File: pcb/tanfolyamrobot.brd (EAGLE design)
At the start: 81.3 x 58.7 mm, 84 parts, among them IC1 STM32F10XRXT6, IC2 7805, IC4 FT232RL, IC5 LD117AS33TR, M1 DRV8833, Q1 AO4407A, Q2 BSS123, Q3 BSS123, Q4 BSS123, X1 CSTCE08M, X2 PWR

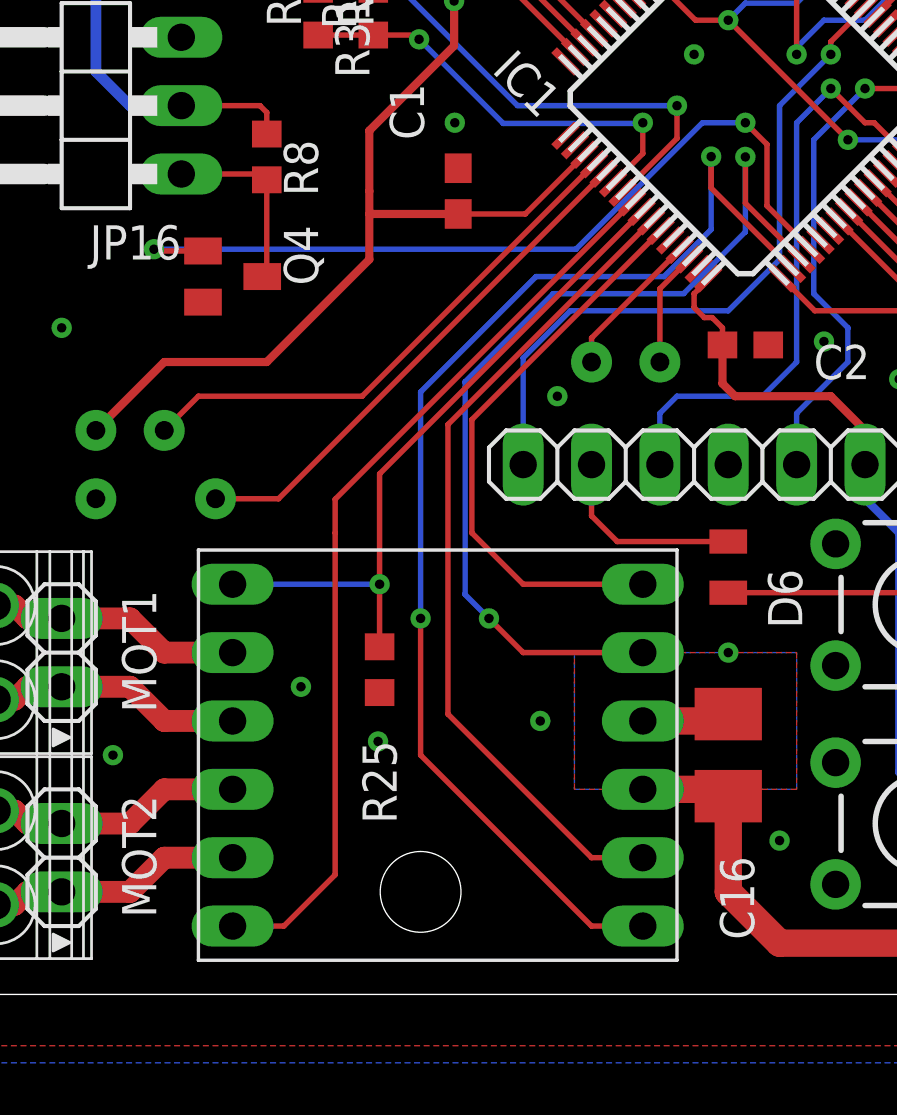
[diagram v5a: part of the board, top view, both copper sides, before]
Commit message: added battery voltage measurement (#1)
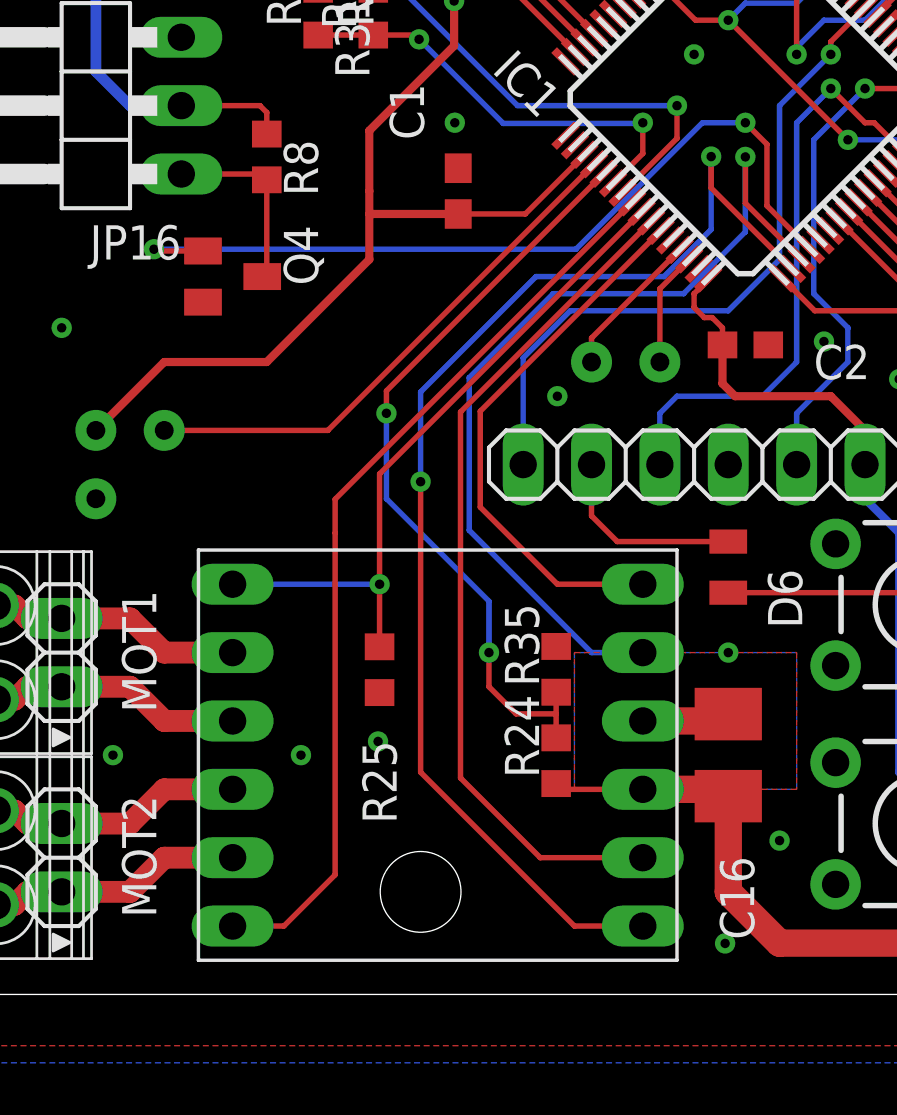
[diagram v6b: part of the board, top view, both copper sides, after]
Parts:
- added R24: 27K, rcl:R0603
- added R35: 6K8, rcl:R0603
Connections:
- removed net PA5: IC1.21
- new net VCC_SENSE: IC1.21, R24.2, R35.1
- net GND: now also R35.2
- net VCC: now also R24.1
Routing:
- net VCC_SENSE: track 0.00 -> 28.6 mm, vias 0 -> 2
- net PA5: track 19.4 -> 0.00 mm, vias 1 -> 0
- net VCC: track 96.3 -> 99.6 mm
- net MOTOR2_IN1: track 35.6 -> 34.0 mm, vias 2 -> 1
- net MOTOR2_IN2: track 21.3 -> 20.3 mm
- net MOTOR1_IN2: track 30.9 -> 31.6 mm
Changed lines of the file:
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@@
 <attribute name="VALUE" x="18.415" y="49.19345" size="1.27" layer="27" rot="R90"/>
+</element>
+<element name="R24" library="rcl" library_urn="urn:adsk.eagle:library:334" package="R0603" package3d_urn="urn:adsk.eagle:package:23555/3" value="27K" x="25.35555" y="8.683625" smashed="yes" rot="R90">
+<attribute name="NAME" x="24.72055" y="8.048625" size="1.27" layer="25" rot="R90"/>
+<attribute name="POPULARITY" value="70" x="25.35555" y="8.683625" size="1.778" layer="27" rot="R90" display="off"/>
+<attribute name="SPICEPREFIX" value="R" x="25.35555" y="8.683625" size="1.778" layer="27" rot="R90" display="off"/>
+<attribute name="VALUE" x="27.26055" y="8.048625" size="1.27" layer="27" rot="R90"/>
+</element>
+<element name="R35" library="rcl" library_urn="urn:adsk.eagle:library:334" package="R0603" package3d_urn="urn:adsk.eagle:package:23555/3" value="6K8" x="25.35555" y="12.0777" smashed="yes" rot="R90">
+<attribute name="NAME" x="24.72055" y="11.4427" size="1.27" layer="25" rot="R90"/>
+<attribute name="POPULARITY" value="70" x="25.35555" y="12.0777" size="1.778" layer="27" rot="R90" display="off"/>
+<attribute name="SPICEPREFIX" value="R" x="25.35555" y="12.0777" size="1.778" layer="27" rot="R90" display="off"/>
+<attribute name="VALUE" x="27.26055" y="11.4427" size="1.27" layer="27" rot="R90"/>
 </element>
 </elements>
@@
 <via x="8.255" y="18.415" extent="1-16" drill="0.7" diameter="1.524"/>
 <via x="6.985" y="38.1" extent="1-16" drill="0.35"/>
-<via x="15.875" y="11.43" extent="1-16" drill="0.35"/>
+<via x="15.875" y="8.89" extent="1-16" drill="0.35"/>
 <via x="18.73885" y="9.398" extent="1-16" drill="0.35"/>
-<via x="24.765" y="10.16" extent="1-16" drill="0.35"/>
+<via x="31.632525" y="1.895475" extent="1-16" drill="0.35"/>
 <via x="31.75" y="12.7" extent="1-16" drill="0.35"/>
 <via x="33.655" y="5.715" extent="1-16" drill="0.35"/>
@@
 <contactref element="R33" pad="2"/>
 <via x="21.59" y="32.385" extent="1-16" drill="0.35"/>
+<contactref element="R35" pad="2"/>
 </signal>
 <signal name="+3V3">
@@
 <wire x1="69.85" y1="23.2918" x2="69.85" y2="21.59" width="0.4064" layer="1"/>
 <wire x1="71.12" y1="23.2918" x2="71.12" y2="20.955" width="0.4064" layer="1"/>
+<contactref element="R24" pad="1"/>
+<wire x1="25.35555" y1="7.833625" x2="25.569175" y2="7.62" width="0.2032" layer="1"/>
+<wire x1="25.569175" y1="7.62" x2="28.575" y2="7.62" width="0.2032" layer="1"/>
 </signal>
 <signal name="N$14">
@@
 <contactref element="M1" pad="IN1"/>
 <via x="31.115" y="31.1277" extent="1-16" drill="0.35"/>
-<via x="20.32" y="13.97" extent="1-16" drill="0.35"/>
-<wire x1="28.575" y1="2.54" x2="26.67" y2="2.54" width="0.2032" layer="1"/>
-<wire x1="20.32" y1="8.89" x2="20.32" y2="13.97" width="0.2032" layer="1"/>
-<wire x1="26.67" y1="2.54" x2="20.32" y2="8.89" width="0.2032" layer="1"/>
+<via x="20.32" y="19.05" extent="1-16" drill="0.35"/>
+<wire x1="28.575" y1="2.54" x2="26.035" y2="2.54" width="0.2032" layer="1"/>
+<wire x1="20.32" y1="8.255" x2="20.32" y2="19.05" width="0.2032" layer="1"/>
+<wire x1="26.035" y1="2.54" x2="20.32" y2="8.255" width="0.2032" layer="1"/>
 <contactref element="IC1" pad="34"/>
 <wire x1="31.115" y1="31.1277" x2="31.115" y2="29.956828125" width="0.2032" layer="1"/>
@@
 <wire x1="24.609425" y1="26.67" x2="29.365575" y2="26.67" width="0.2032" layer="16"/>
 <wire x1="31.115" y1="28.419425" x2="31.115" y2="31.1277" width="0.2032" layer="16"/>
-<wire x1="20.32" y1="13.97" x2="20.32" y2="22.380575" width="0.2032" layer="16"/>
+<wire x1="20.32" y1="19.05" x2="20.32" y2="22.380575" width="0.2032" layer="16"/>
 <wire x1="29.365575" y1="26.67" x2="31.115" y2="28.419425" width="0.2032" layer="16"/>
 </signal>
@@
 <contactref element="M1" pad="IN2"/>
 <contactref element="IC1" pad="26"/>
-<wire x1="21.336" y1="10.414" x2="26.67" y2="5.08" width="0.2032" layer="1"/>
-<wire x1="26.67" y1="5.08" x2="28.575" y2="5.08" width="0.2032" layer="1"/>
-<wire x1="28.88481875" y1="28.722184375" x2="21.336" y2="21.173365625" width="0.2032" layer="1"/>
-<wire x1="21.336" y1="21.173365625" x2="21.336" y2="10.414" width="0.2032" layer="1"/>
+<wire x1="21.802725" y1="8.042275" x2="24.765" y2="5.08" width="0.2032" layer="1"/>
+<wire x1="24.765" y1="5.08" x2="28.575" y2="5.08" width="0.2032" layer="1"/>
+<wire x1="28.88481875" y1="28.722184375" x2="21.802725" y2="21.640090625" width="0.2032" layer="1"/>
+<wire x1="21.802725" y1="21.640090625" x2="21.802725" y2="8.042275" width="0.2032" layer="1"/>
 </signal>
 <signal name="MOTOR2_IN1">
 <contactref element="M1" pad="IN3"/>
-<wire x1="28.575" y1="12.7" x2="24.13" y2="12.7" width="0.2032" layer="1"/>
-<wire x1="24.13" y1="12.7" x2="22.86" y2="13.97" width="0.2032" layer="1"/>
-<via x="22.86" y="13.97" extent="1-16" drill="0.35"/>
 <via x="32.385" y="31.115" extent="1-16" drill="0.35"/>
-<wire x1="22.86" y1="13.97" x2="21.971" y2="14.859" width="0.2032" layer="16"/>
 <contactref element="IC1" pad="35"/>
 <wire x1="32.385" y1="31.115" x2="32.385" y2="29.393934375" width="0.2032" layer="1"/>
 <wire x1="34.4709625" y1="27.307971875" x2="32.385" y2="29.393934375" width="0.2032" layer="1"/>
-<wire x1="21.971" y1="22.761575" x2="25.244425" y2="26.035" width="0.2032" layer="16"/>
+<wire x1="22.126575" y1="22.91715" x2="25.244425" y2="26.035" width="0.2032" layer="16"/>
 <wire x1="25.244425" y1="26.035" x2="30.09265" y2="26.035" width="0.2032" layer="16"/>
 <wire x1="32.385" y1="28.32735" x2="30.09265" y2="26.035" width="0.2032" layer="16"/>
 <wire x1="32.385" y1="28.32735" x2="32.385" y2="31.115" width="0.2032" layer="16"/>
-<wire x1="21.971" y1="14.859" x2="21.971" y2="22.761575" width="0.2032" layer="16"/>
+<wire x1="22.126575" y1="17.243425" x2="22.126575" y2="22.91715" width="0.2032" layer="16"/>
+<wire x1="28.575" y1="12.7" x2="26.67" y2="12.7" width="0.2032" layer="16"/>
+<wire x1="26.67" y1="12.7" x2="22.126575" y2="17.243425" width="0.2032" layer="16"/>
 </signal>
 <signal name="MOTOR2_IN2">
 <contactref element="M1" pad="IN4"/>
 <contactref element="IC1" pad="27"/>
-<wire x1="28.575" y1="15.24" x2="24.13" y2="15.24" width="0.2032" layer="1"/>
-<wire x1="29.238371875" y1="28.36863125" x2="22.225" y2="21.355259375" width="0.2032" layer="1"/>
-<wire x1="22.225" y1="21.355259375" x2="22.225" y2="17.145" width="0.2032" layer="1"/>
-<wire x1="22.225" y1="17.145" x2="24.13" y2="15.24" width="0.2032" layer="1"/>
+<wire x1="28.575" y1="15.24" x2="25.4" y2="15.24" width="0.2032" layer="1"/>
+<wire x1="29.238371875" y1="28.36863125" x2="22.53615" y2="21.666409375" width="0.2032" layer="1"/>
+<wire x1="22.53615" y1="21.666409375" x2="22.53615" y2="18.10385" width="0.2032" layer="1"/>
+<wire x1="22.53615" y1="18.10385" x2="25.4" y2="15.24" width="0.2032" layer="1"/>
 </signal>
 <signal name="MOTOR_SLEEPN">
@@
 <contactref element="IC1" pad="20"/>
 <via x="10.795" y="20.955" extent="1-16" drill="0.7" diameter="1.524"/>
-<wire x1="12.065" y1="22.225" x2="10.795" y2="20.955" width="0.2032" layer="1"/>
-<wire x1="26.7635" y1="30.84350625" x2="18.14499375" y2="22.225" width="0.2032" layer="1"/>
-<wire x1="18.14499375" y1="22.225" x2="12.065" y2="22.225" width="0.2032" layer="1"/>
-</signal>
-<signal name="PA5">
-<contactref element="IC1" pad="21"/>
-<via x="12.7" y="18.415" extent="1-16" drill="0.7" diameter="1.524"/>
-<wire x1="15.0421" y1="18.415" x2="12.7" y2="18.415" width="0.2032" layer="1"/>
-<wire x1="27.117053125" y1="30.489953125" x2="15.0421" y2="18.415" width="0.2032" layer="1"/>
+<wire x1="26.7635" y1="30.84350625" x2="16.87499375" y2="20.955" width="0.2032" layer="1"/>
+<wire x1="16.87499375" y1="20.955" x2="10.795" y2="20.955" width="0.2032" layer="1"/>
 </signal>
 <signal name="SERVO_5V">
@@
 <wire x1="14.72655" y1="37.34345" x2="16.513175" y2="37.34345" width="0.2032" layer="1"/>
 </signal>
+<signal name="VCC_SENSE">
+<contactref element="R24" pad="2"/>
+<contactref element="R35" pad="1"/>
+<wire x1="25.35555" y1="9.533625" x2="25.35555" y2="10.423525" width="0.2032" layer="1"/>
+<wire x1="25.35555" y1="11.2277" x2="25.35555" y2="10.423525" width="0.2032" layer="1"/>
+<wire x1="23.866475" y1="10.423525" x2="22.86" y2="11.43" width="0.2032" layer="1"/>
+<wire x1="23.866475" y1="10.423525" x2="25.35555" y2="10.423525" width="0.2032" layer="1"/>
+<wire x1="22.86" y1="11.43" x2="22.86" y2="12.7" width="0.2032" layer="1"/>
+<via x="22.86" y="12.7" extent="1-16" drill="0.35"/>
+<wire x1="22.86" y1="12.7" x2="22.86" y2="14.605" width="0.2032" layer="16"/>
+<wire x1="22.86" y1="14.605" x2="19.05" y2="18.415" width="0.2032" layer="16"/>
+<wire x1="19.05" y1="18.415" x2="19.05" y2="21.59" width="0.2032" layer="16"/>
+<via x="19.05" y="21.59" extent="1-16" drill="0.35"/>
+<contactref element="IC1" pad="21"/>
+<wire x1="27.117053125" y1="30.489953125" x2="19.05" y2="22.4229" width="0.2032" layer="1"/>
+<wire x1="19.05" y1="22.4229" x2="19.05" y2="21.59" width="0.2032" layer="1"/>
+</signal>
 </signals>

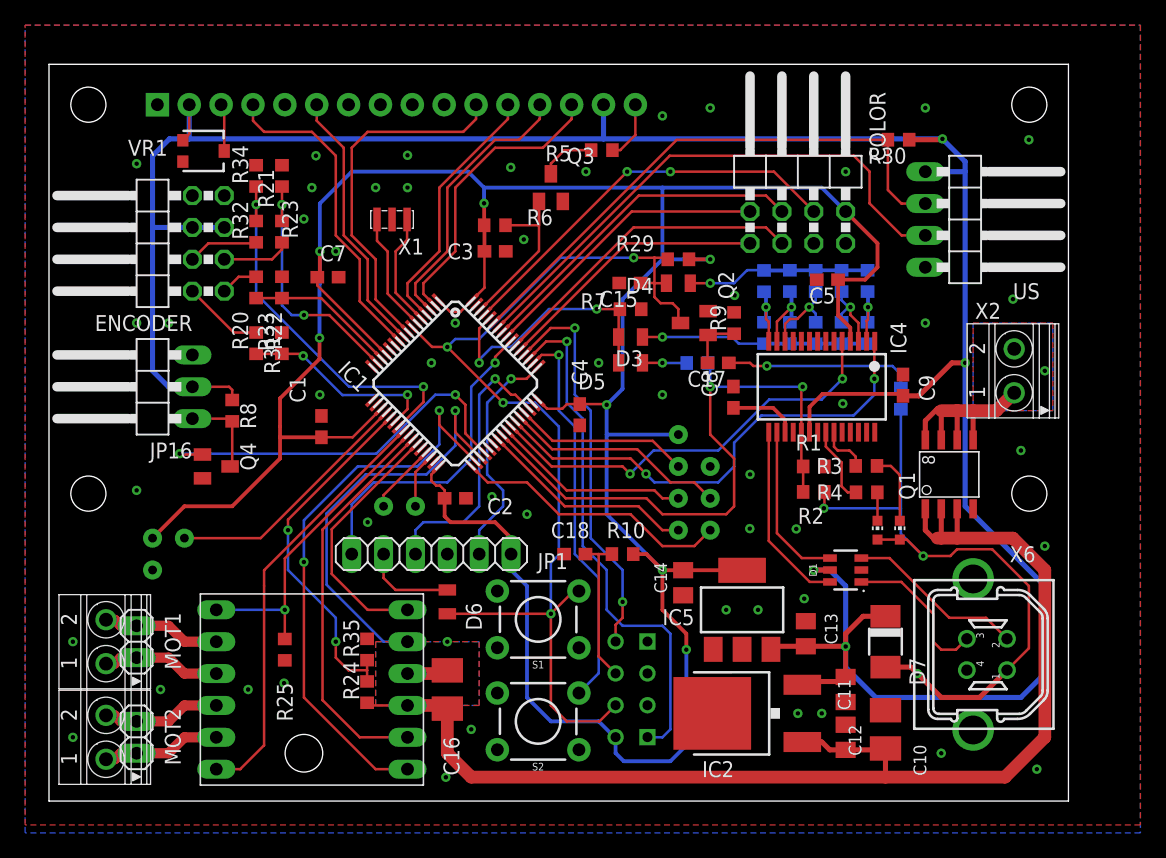
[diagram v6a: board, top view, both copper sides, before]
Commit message: fixed unused pins' headers
also had to move some stuff around
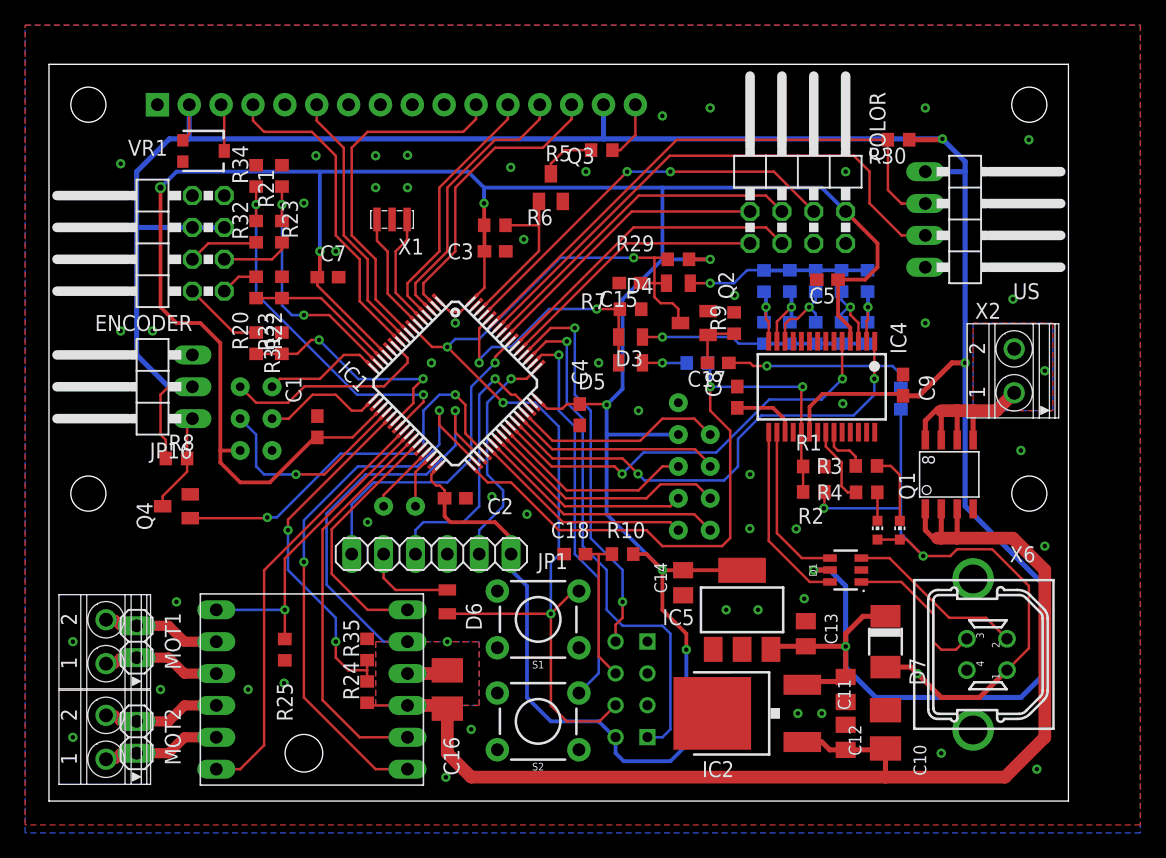
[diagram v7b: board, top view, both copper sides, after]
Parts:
- moved R8 5.85 mm to (10.2, 27.3), turned to 0 degrees
- moved Q4 4.49 mm to (10.2, 23.5), turned to 90 degrees
- moved C1 0.32 mm to (21.4, 29.8)
- moved C8 0.31 mm to (54.9, 32.2)
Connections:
- net N$6 renamed LCD_K
- removed net PB12: IC1.33
- new net PA2: IC1.16
- new net PA3: IC1.17
- new net PC9: IC1.40
- net USB_PWR_DET: now also IC1.33; no longer IC1.40
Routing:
- net PB12: track 22.1 -> 0.00 mm, vias 1 -> 0
- net PC7: track 0.00 -> 20.0 mm, vias 0 -> 1
- net PC9: track 0.00 -> 19.4 mm, vias 0 -> 1
- net +3V3: track 240.7 -> 258.5 mm
- net PC6: track 0.00 -> 17.6 mm, vias 0 -> 1
- net PC3: track 0.00 -> 17.1 mm, vias 0 -> 1
- net PA3: track 0.00 -> 9.56 mm, vias 0 -> 1
- net PA2: track 0.00 -> 9.35 mm, vias 0 -> 1
- net +5V: track 216.0 -> 222.3 mm
- net USB_PWR_DET: track 49.3 -> 53.9 mm
- net ENC2_A_3V3: track 16.1 -> 19.6 mm
- net PA4: track 20.1 -> 16.8 mm, vias 1 -> 2
- net PA12: track 13.9 -> 16.8 mm
- net SERVO: track 31.5 -> 32.7 mm
- net SERVO_5V: track 6.93 -> 7.97 mm
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
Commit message: fixed silkscreen
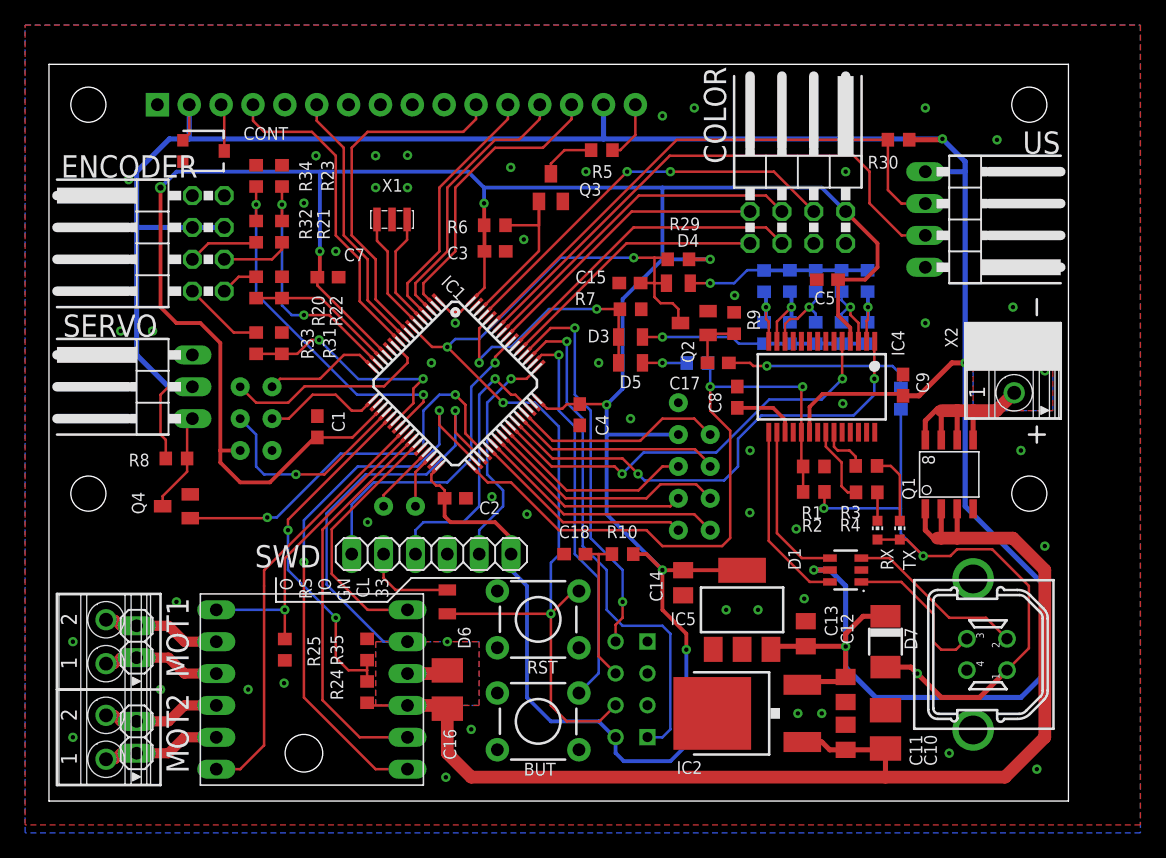
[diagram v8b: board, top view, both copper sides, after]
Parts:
- renumbered JP1 to SWD, JP16 to SERVO, LED1 to TX, LED2 to RX, S1 to RST, S2 to BUT, VR1 to CONT
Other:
- board text added: "GND 3V3 PA8 PC8 PC6"
- board text added: "O RS IO GN CL 33"
- board text added: "PA12 PA11 PC9 PC7"
- board text added: "PA2 PC3 PA3 PA4 GND 3V3"
- board text removed: "+3V3 PC9 PB15"
- board text removed: "3V3 PA5 PA7"
- board text removed: "GND PA4 PA6"
- board text removed: "GND PC8 PB12"
- board text removed: "PA8 PA11 PA12"
